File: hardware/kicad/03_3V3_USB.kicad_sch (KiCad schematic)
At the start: 0 parts

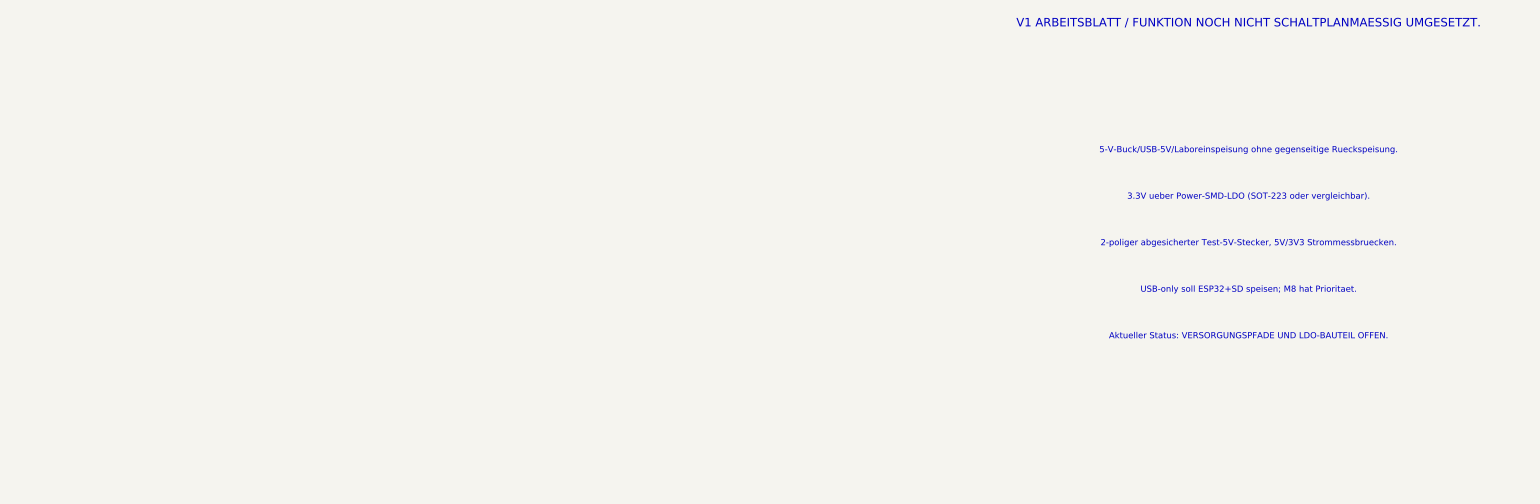
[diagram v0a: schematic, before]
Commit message: hardware(usb): implement TPS2116 M8 first power mux and NCV1117 3.3V core rail
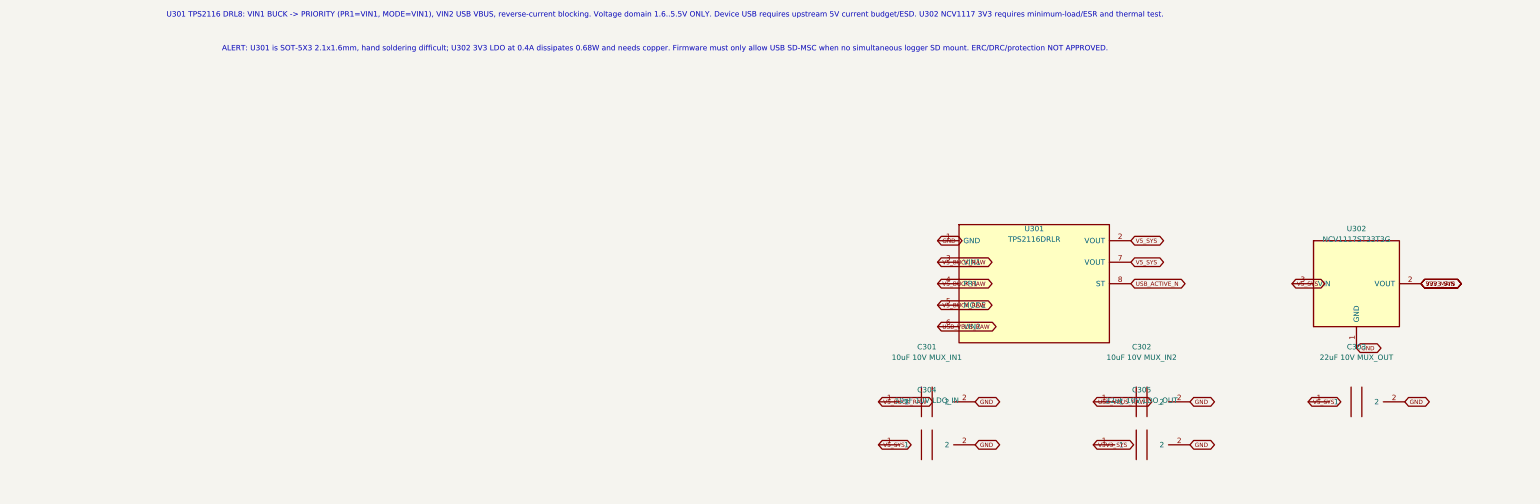
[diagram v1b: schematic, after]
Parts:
- added C301: 10uF 10V MUX_IN1, Tripmaster:C_1210_3225, symbol Tripmaster_Sym:C
- added C302: 10uF 10V MUX_IN2, Tripmaster:C_1210_3225, symbol Tripmaster_Sym:C
- added C303: 22uF 10V MUX_OUT, Tripmaster:C_1210_3225, symbol Tripmaster_Sym:C
- added C304: 10uF 10V LDO_IN, Tripmaster:C_1210_3225, symbol Tripmaster_Sym:C
- added C305: 22uF 10V LDO_OUT, Tripmaster:C_1210_3225, symbol Tripmaster_Sym:C
- added U301: TPS2116DRLR, Tripmaster:TPS2116_DRL0008A, symbol TripTracer_V1:TPS2116_DRL8
- added U302: NCV1117ST33T3G, Package_TO_SOT_SMD:SOT-223-3_TabPin2, symbol TripTracer_V1:NCV1117_3V3
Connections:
- new net 3V3_MAIN: C305.1, U302.2 (VOUT)
- new net GND: C301.2, C302.2, C303.2, C304.2, C305.2, U301.1 (GND), U302.1 (GND)
- new net USB_ACTIVE_N: U301.8 (ST)
- new net USB_VBUS_RAW: C302.1, U301.6 (VIN2)
- new net V5_BUCK_RAW: C301.1, U301.3 (VIN1), U301.4 (PR1), U301.5 (MODE)
- new net V5_SYS: C303.1, C304.1, U301.2 (VOUT), U301.7 (VOUT), U302.3 (VIN)
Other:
- note added: "ALERT: U301 is SOT-5X3 2.1x1.6mm, hand soldering difficult; U302 3V3 LDO at 0.4A dissipates 0.68W and needs copper. Firmware must only allow USB SD-MSC when no simultaneous logger SD mount. ERC/DRC/protection NOT APPROVED."
- note added: "U301 TPS2116 DRL8: VIN1 BUCK -> PRIORITY (PR1=VIN1, MODE=VIN1), VIN2 USB VBUS, reverse-current blocking. Voltage domain 1.6..5.5V ONLY. Device USB requires upstream 5V current budget/ESD. U302 NCV1117 3V3 requires minimum-load/ESR and thermal test."
- note removed: "2-poliger abgesicherter Test-5V-Stecker, 5V/3V3 Strommessbruecken."
- note removed: "3.3V ueber Power-SMD-LDO (SOT-223 oder vergleichbar)."
- note removed: "5-V-Buck/USB-5V/Laboreinspeisung ohne gegenseitige Rueckspeisung."
- note removed: "Aktueller Status: VERSORGUNGSPFADE UND LDO-BAUTEIL OFFEN."
- note removed: "USB-only soll ESP32+SD speisen; M8 hat Prioritaet."
- note removed: "V1 ARBEITSBLATT / FUNKTION NOCH NICHT SCHALTPLANMAESSIG UMGESETZT."
- title: TripTracer V1 – 3,3-V-LDO / USB- und Laboreinspeisung -> TripTracer 3V3 and USB-M8 priority power path
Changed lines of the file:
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@@
-(kicad_sch (version 20250114) (generator "eeschema")
- (paper "A3") (title_block (title "TripTracer V1 – 3,3-V-LDO / USB- und Laboreinspeisung") (date "2026-10-13") (rev "a0 / NOCH NICHT VERDRAHTET"))
- (text "V1 ARBEITSBLATT / FUNKTION NOCH NICHT SCHALTPLANMAESSIG UMGESETZT." (at 165 35 0) (effects (font (size 2 2))))
- (text "5-V-Buck/USB-5V/Laboreinspeisung ohne gegenseitige Rueckspeisung." (at 165 65 0) (effects (font (size 1.45 1.45))))
-(text "3.3V ueber Power-SMD-LDO (SOT-223 oder vergleichbar)." (at 165 76 0) (effects (font (size 1.45 1.45))))
-(text "2-poliger abgesicherter Test-5V-Stecker, 5V/3V3 Strommessbruecken." (at 165 87 0) (effects (font (size 1.45 1.45))))
-(text "USB-only soll ESP32+SD speisen; M8 hat Prioritaet." (at 165 98 0) (effects (font (size 1.45 1.45))))
-(text "Aktueller Status: VERSORGUNGSPFADE UND LDO-BAUTEIL OFFEN." (at 165 109 0) (effects (font (size 1.45 1.45))))
- (sheet_instances (path "/" (page "4"))) (embedded_fonts no)
-)

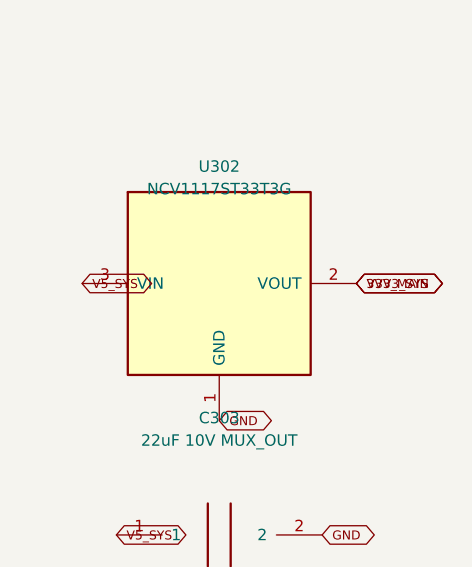
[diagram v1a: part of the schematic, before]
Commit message: hardware(usb): remove duplicate 3V3 alias after timer switched to V3V3_SYS
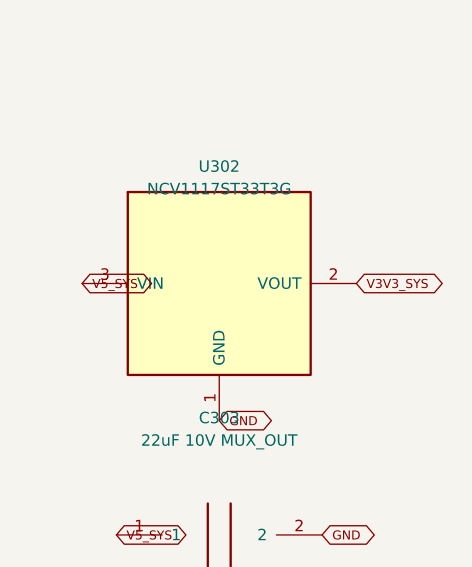
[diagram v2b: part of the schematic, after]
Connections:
- net 3V3_MAIN renamed V3V3_SYS

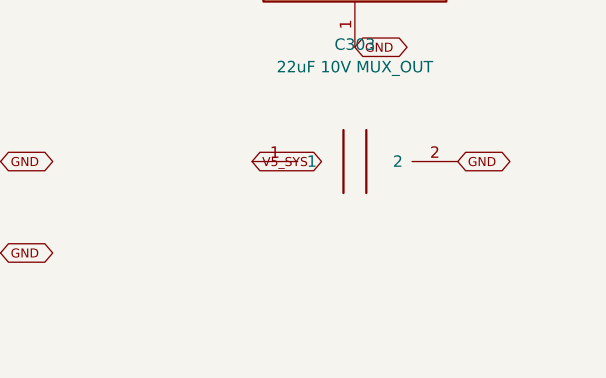
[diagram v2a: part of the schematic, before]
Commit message: hardware(usb): add 3.3V pullup to TPS2116 ST output for ESP32 USB-only detect
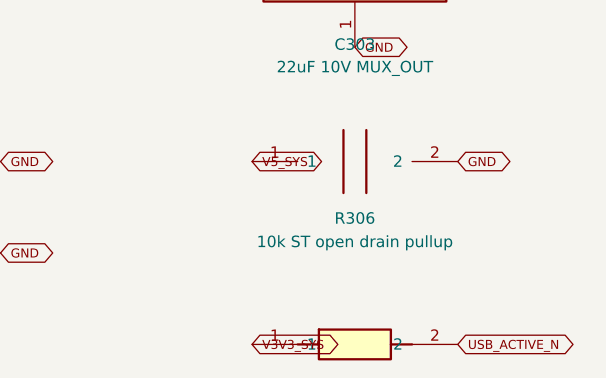
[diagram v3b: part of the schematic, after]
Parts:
- added R306: 10k ST open drain pullup, Tripmaster:R_1206_3216, symbol Tripmaster_Sym:R
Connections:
- net USB_ACTIVE_N: now also R306.2
- net V3V3_SYS: now also R306.1
